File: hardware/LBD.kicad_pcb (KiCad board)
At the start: 2 copper layers, 39 parts, among them Q1 AO3400A, Q2 AO3400A, U1 RP2040-ZERO

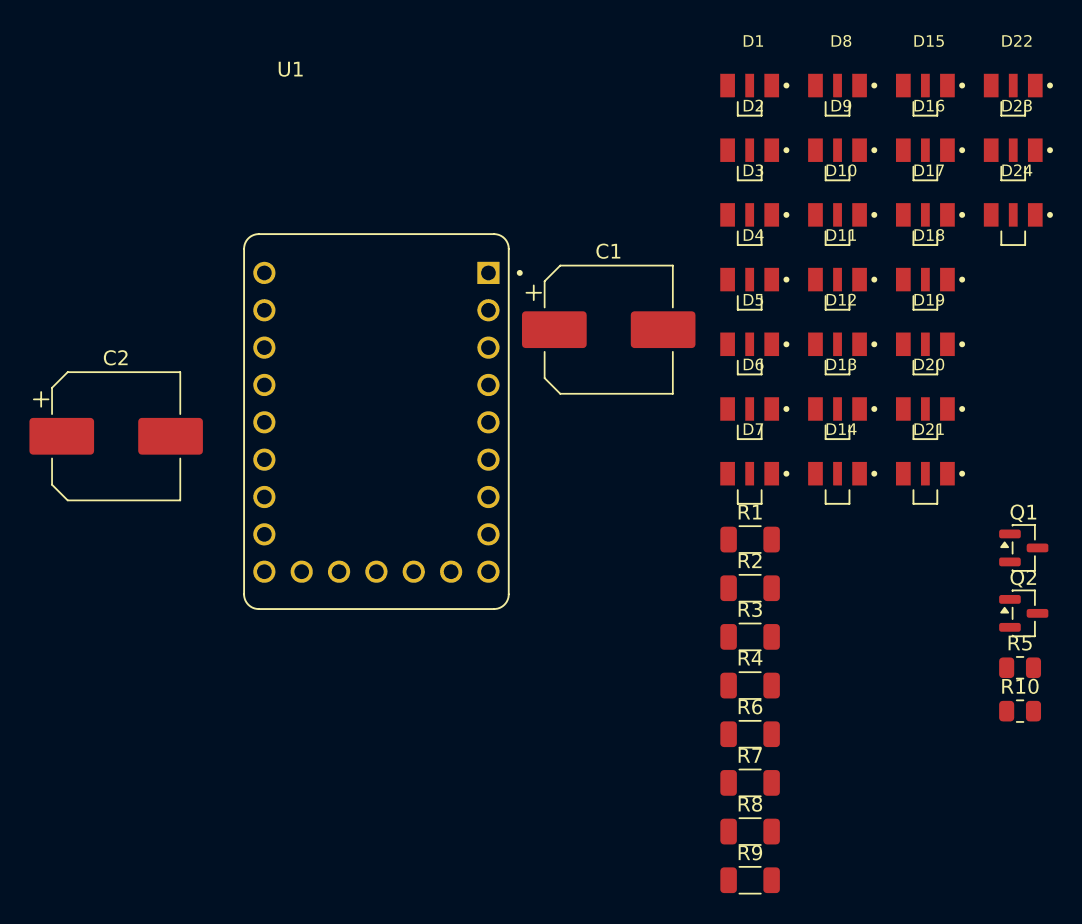
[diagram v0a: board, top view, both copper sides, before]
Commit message: started placing leds
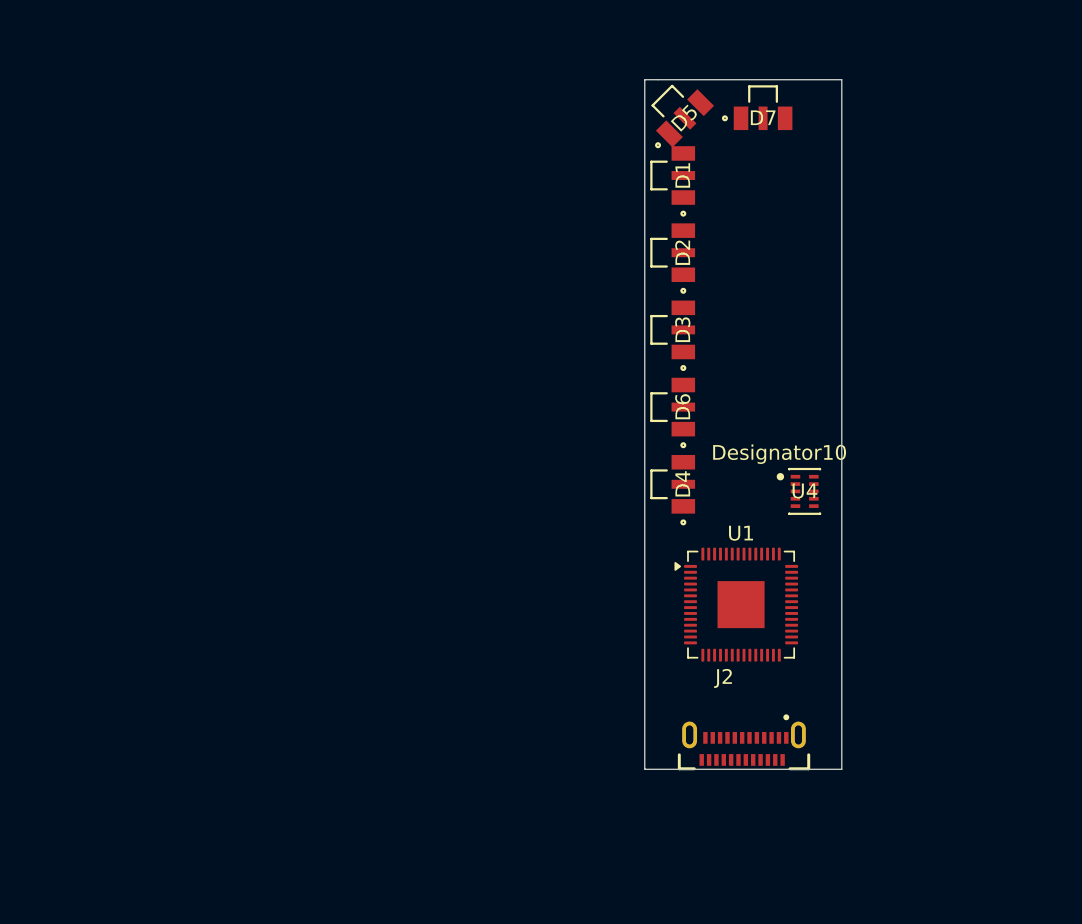
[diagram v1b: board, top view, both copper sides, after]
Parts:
- removed C1, C2: 470u, Capacitor_SMD:CP_Elec_8x10.5
- removed D10, D11, D12, D13, D14, D15, D16, D17, D18, D19, D20, D21, D22, D23, D24, D8, D9: IN-S126ESGHIR, IN_S126ESGHIR:LED_IN-S126ESGHIR
- removed Q1, Q2: AO3400A, Package_TO_SOT_SMD:SOT-23
- removed R1, R2, R3, R4, R6, R7, R8, R9: 6.2, Resistor_SMD:R_1206_3216Metric
- removed R10, R5: 10K, Resistor_SMD:R_0805_2012Metric
- added J2: USB4155-03-C_REVA, LBD_Footprints:GCT_USB4155-03-C_REVA, F.Cu at (147.0, 124.0)
- added U4: TPSM828214SILR, LBD_Footprints:TPSM828214SILR, F.Cu at (151.1, 106.5)
- D1, D2, D3, D4, D5, D6, D7: value IN-S126ESGHIR -> LED; footprint IN_S126ESGHIR:LED_IN-S126ESGHIR -> LBD_Footprints:LED_IN-S12_INL
- U1: value RP2040-ZERO -> RP2040; footprint RP2040-ZERO:MODULE_RP2040-ONE -> Package_DFN_QFN:QFN-56-1EP_7x7mm_P0.4mm_EP3.2x3.2mm
- moved U1 28.2 mm to (146.8, 114.2)
- moved D7 24.2 mm to (148.3, 81.1)
- moved D5 16.0 mm to (143.0, 81.1), turned to 45 degrees
- moved D4 14.6 mm to (142.9, 106.0), turned to 90 degrees
- moved D3 9.03 mm to (142.9, 95.5), turned to 90 degrees
- moved D2 8.30 mm to (142.9, 90.3), turned to 90 degrees
- moved D1 7.60 mm to (142.9, 85.0), turned to 90 degrees
- moved D6 4.51 mm to (142.9, 100.8), turned to 90 degrees
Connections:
- D1 pad 1: Net-(D1-Pad1) -> unconnected-(D1-K-Pad1)
- D1 pad 2: Net-(D1-Pad2) -> unconnected-(D1-A-Pad2)
- D2 pad 1: Net-(D1-Pad2) -> unconnected-(D2-K-Pad1)
- D2 pad 2: Net-(D2-Pad2) -> unconnected-(D2-A-Pad2)
- D3 pad 1: Net-(D2-Pad2) -> unconnected-(D3-K-Pad1)
- D3 pad 2: Net-(Q2-D) -> unconnected-(D3-A-Pad2)
- D4 pad 1: Net-(D4-Pad1) -> unconnected-(D4-K-Pad1)
- D4 pad 2: Net-(D4-Pad2) -> unconnected-(D4-A-Pad2)
- D5 pad 1: Net-(D4-Pad2) -> unconnected-(D5-K-Pad1)
- D5 pad 2: Net-(D5-Pad2) -> unconnected-(D5-A-Pad2)
- D6 pad 1: Net-(D5-Pad2) -> unconnected-(D6-K-Pad1)
- D6 pad 2: Net-(Q2-D) -> unconnected-(D6-A-Pad2)
- D7 pad 1: Net-(D7-Pad1) -> unconnected-(D7-K-Pad1)
- D7 pad 2: Net-(D7-Pad2) -> unconnected-(D7-A-Pad2)
- U1 pad 1: unconnected-(U1-GP0-Pad1) -> +3.3V
- U1 pad 10: unconnected-(U1-GP9-Pad10) -> +3.3V
- U1 pad 17: LEFT_FRONT -> unconnected-(U1-GPIO14-Pad17)
- U1 pad 19: unconnected-(U1-GP28-Pad19) -> GND
- U1 pad 20: unconnected-(U1-GP29-Pad20) -> Net-(U1-XIN)
- U1 pad 21: unconnected-(U1-3V3-Pad21) -> Net-(U1-XOUT)
- U1 pad 22: GND -> +3.3V
- U1 pad 23: +5V -> +1V1
- U1 pad 7: RIGHT_FRONT -> unconnected-(U1-GPIO5-Pad7)
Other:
- board outline added: 13.4 x 46.9 mm
